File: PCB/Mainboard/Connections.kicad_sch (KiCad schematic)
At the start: 37 parts, among them J10 I2C, J11 Servo 0, J12 Servo 1, J13 PW_IO_bak, J14 PW_IO_bak, J15 Servo 4, J16 Servo 5, J17 Servo 2, J18 Servo 3, J19 Servo 6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

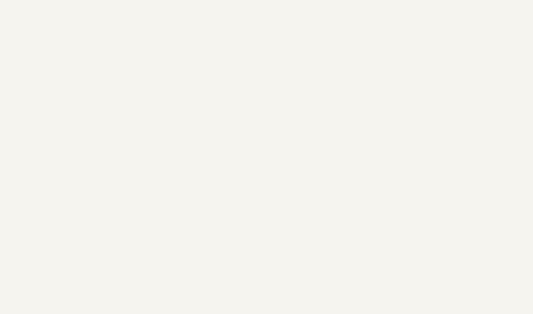
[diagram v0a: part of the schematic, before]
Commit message: Added setup, read and get Command
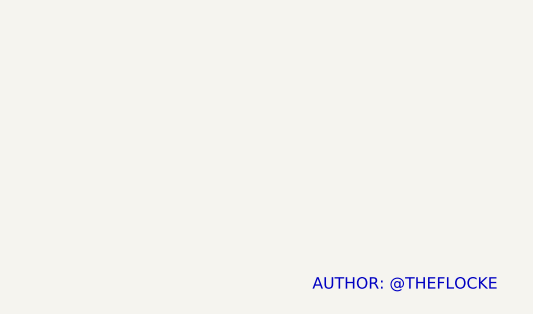
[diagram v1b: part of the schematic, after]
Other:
- note added: "AUTHOR: @THEFLOCKE"
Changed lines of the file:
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@@
+		)
+	)
+	(text "AUTHOR: @THEFLOCKE"
+		(exclude_from_sim no)
+		(at 249.936 196.596 0)
+		(effects
+			(font
+				(face "KiCad Font")
+				(size 1.27 1.27)
+				(color 194 0 194 1)
+			)
 		)
 	)

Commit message: Fixed Grammar
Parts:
- removed D4: LED, Diode_SMD:D_0805_2012Metric_Pad1.15x1.40mm_HandSolder, symbol Device:LED
- removed J6: Micro_SD_Card_Det_Hirose_DM3AT, Connector_Card:microSD_HC_Hirose_DM3D-SF, symbol Connector:Micro_SD_Card_Det_Hirose_DM3AT
- removed R32, R34, R35, R36: 10k, Resistor_SMD:R_0805_2012Metric_Pad1.20x1.40mm_HandSolder, symbol Device:R
- removed R33: 15, Resistor_SMD:R_0805_2012Metric_Pad1.20x1.40mm_HandSolder, symbol Device:R
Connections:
- no-connect marks 2 -> 0
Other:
- moved on the sheet: C19, C20, C21, C22, C23, C24, C25, C26, J10, J11, J12, J13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

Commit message: upload images and deleted pcb new
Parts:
- added D4: LED, Diode_SMD:D_0805_2012Metric_Pad1.15x1.40mm_HandSolder, symbol Device:LED
- added J6: Micro_SD_Card_Det_Hirose_DM3AT, Connector_Card:microSD_HC_Hirose_DM3D-SF, symbol Connector:Micro_SD_Card_Det_Hirose_DM3AT
- added R32, R34, R35, R36: 10k, Resistor_SMD:R_0805_2012Metric_Pad1.20x1.40mm_HandSolder, symbol Device:R
- added R33: 15, Resistor_SMD:R_0805_2012Metric_Pad1.20x1.40mm_HandSolder, symbol Device:R
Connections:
- net GND: now also J6.11 (SHIELD), J6.6 (VSS), J6.9 (DET_B)
- net SPI_SCK: now also J6.5 (CLK), R34.1
- net SPI_SDI: now also J6.7 (DAT0), R32.1
- net SPI_SDO: now also J6.3 (CMD), R35.1
- net VCC_3V3: now also J6.4 (VDD), R32.2, R33.2, R34.2, R35.2, R36.2
- new net: D4.1 (K), J6.10 (DET_A)
- new net: D4.2 (A), R33.1
- new net SD_CSB: J6.2 (DAT3/CD), R36.1
- no-connect marks 0 -> 2
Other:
- moved on the sheet: C19, C20, C21, C22, C23, C24, C25, C26, J10, J11, J12, J13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
